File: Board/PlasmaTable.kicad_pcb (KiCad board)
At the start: 2 copper layers, 99.1 x 86.4 mm, 48 parts, among them P1 CONN_20X2, P10 CONN_1, P11 CONN_1, P2 CONN_5, P3 CONN_5, P4 CONN_5, P5 CONN_5, P6 CONN_5, P7 CONN_5, P8 CONN_1, P9 CONN_1, Q1 TIP120, Q2 TIP120, Q3 TIP120, U1 7805, U2 7805, U3 7805, U4 7805

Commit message: Plotted PCB
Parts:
- C1, C4: value C -> 47 uF
- C2, C5: value C -> 100 uF
- C3, C6: value C -> 1000 uF
- C7, C8, C9: value C -> 0.1 uF
- R1, R12, R8: value R -> 51K
- R10, R14, R3, R5, R6, R7: value R -> 10K
- R11, R13, R15, R2, R4, R9: value R -> 0.2 Ohm
- moved DRV1 36.5 mm to (157.5, 99.1)
- moved DRV3 29.6 mm to (127.0, 99.1)
- moved D2 6.50 mm to (148.0, 115.9), turned to 180 degrees
- moved D1 6.46 mm to (161.9, 116.0), turned to 180 degrees
- moved D3 5.88 mm to (134.9, 116.0), turned to 180 degrees
- moved DRV2 3.44 mm to (142.2, 99.1)
- moved R1 3.24 mm to (172.7, 98.2)
- moved R10 3.24 mm to (172.7, 108.3)
- moved R11 3.24 mm to (172.7, 90.5)
- moved R12 3.24 mm to (172.7, 121.0)
- moved R13 3.24 mm to (172.7, 95.6)
- moved R15 3.24 mm to (172.7, 85.5)
- moved R2 3.24 mm to (172.7, 100.7)
- moved R3 3.24 mm to (172.7, 103.2)
- moved R6 3.24 mm to (172.7, 118.5)
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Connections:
- P2 pad 2: /OUT1B_X -> /OUT2A_X
- P2 pad 3: /OUT2A_X -> /OUT1B_X
- P3 pad 2: /OUT1B_Y -> /OUT2A_Y
- P3 pad 3: /OUT2A_Y -> /OUT1B_Y
- P4 pad 2: /OUT1B_Z -> /OUT2A_Z
- P4 pad 3: /OUT2A_Z -> /OUT1B_Z
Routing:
- net GND: track 0.00 -> 1024.8 mm, vias 0 -> 6
- net Net-(DRV1-Pad23): track 0.00 -> 435.7 mm, vias 0 -> 2
- net /AUX1_BASE: track 0.00 -> 212.0 mm
- net VCC: track 0.00 -> 199.4 mm, vias 0 -> 8
- net /AUX2: track 0.00 -> 194.8 mm
- net +5V: track 0.00 -> 175.4 mm, vias 0 -> 5
- net /AUX1: track 0.00 -> 164.8 mm
- net /SWITCH2: track 0.00 -> 149.8 mm, vias 0 -> 2
- net Net-(DRV3-Pad15): track 0.00 -> 139.0 mm, vias 0 -> 2
- net Net-(DRV3-Pad11): track 0.00 -> 138.4 mm, vias 0 -> 2
- net /SWITCH3: track 0.00 -> 135.7 mm, vias 0 -> 2
- net /SWITCH1: track 0.00 -> 133.2 mm
- net /Z_ENABLE: track 0.00 -> 130.5 mm
- net Net-(Q2-Pad1): track 0.00 -> 116.4 mm
- net Net-(DRV2-Pad11): track 0.00 -> 112.3 mm, vias 0 -> 3
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- added copper zone on B.Cu, net GND
- added copper zone on F.Cu, net GND
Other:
- rule trace_min: 0.2 -> 0.1016
- board text added: "1"
- board text added: "5V"
- board text added: "A+"
- board text added: "A-"
- board text added: "AUX"
- board text added: "B+"
- board text added: "B-"
- board text added: "DISCRETE"
- board text added: "G"
- board text added: "S1"
- board text added: "S2"
- board text added: "S3"
- board text added: "SWITCHES"
- board text added: "V+"
- board text added: "VIN"
- board text added: "X AXIS"
- board text added: "X1"
- board text added: "X2"
- board text added: "X3"
- board text added: "Y AXIS"
- board text added: "Z AXIS"

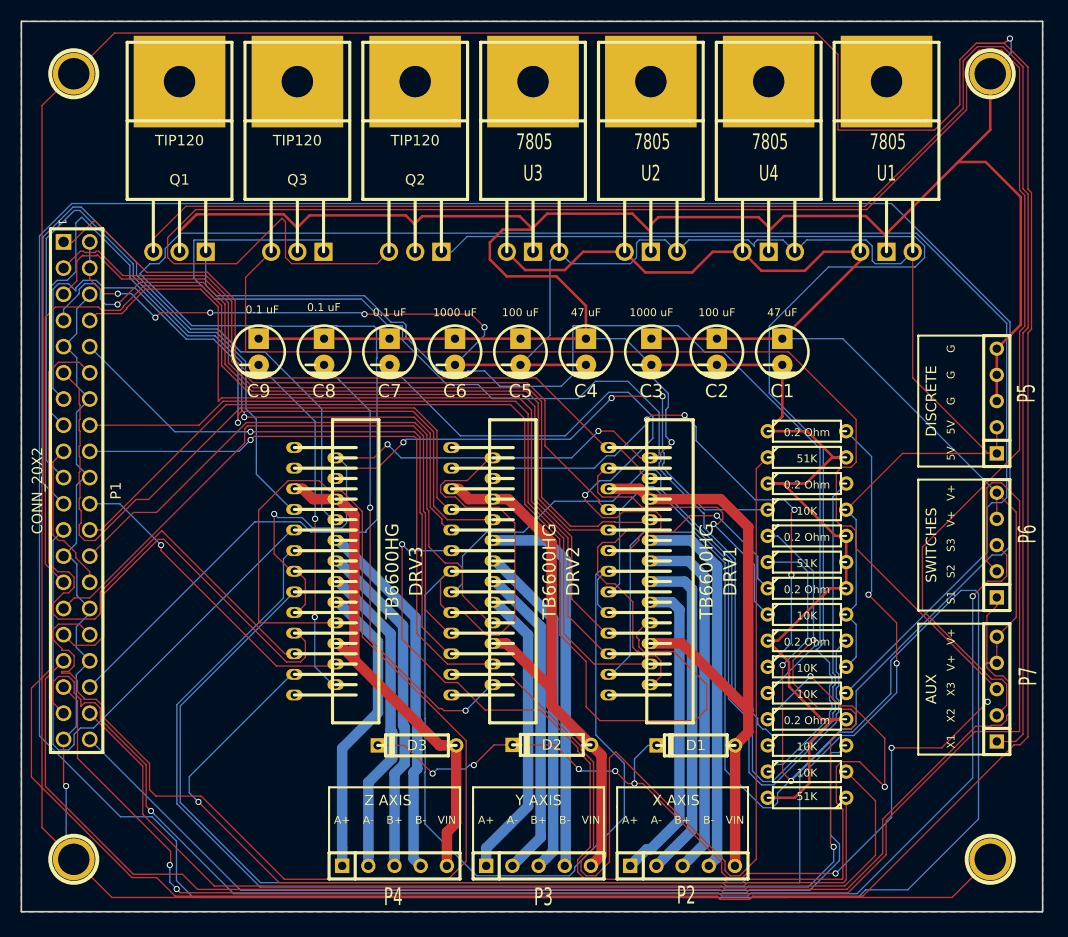
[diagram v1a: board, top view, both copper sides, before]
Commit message: Fixed errors made in first revision and plotted
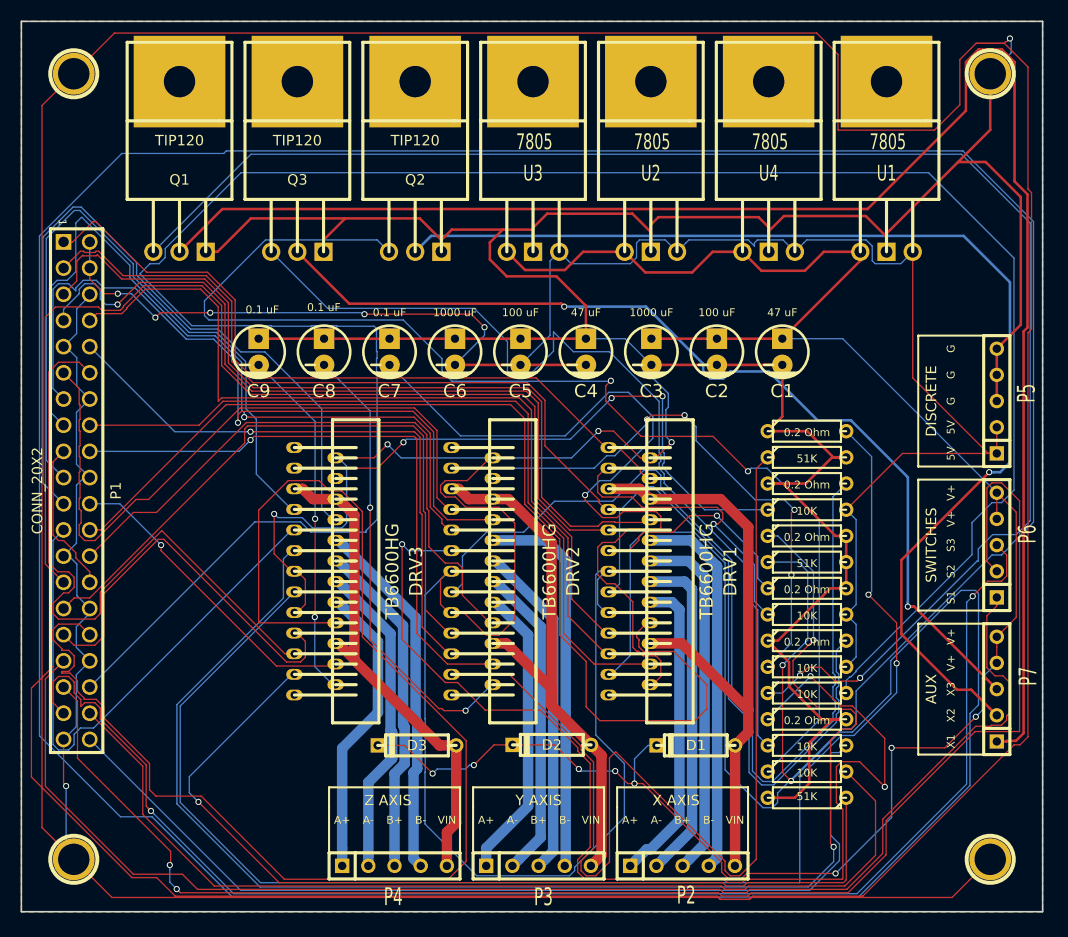
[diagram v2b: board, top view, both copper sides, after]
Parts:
- Q1, Q2, Q3: footprint discret:TO220 -> PlasmaTable:TO220
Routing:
- net /AUX2: track 194.8 -> 111.8 mm, vias 0 -> 1
- net Net-(Q1-Pad1): track 104.2 -> 154.8 mm, vias 0 -> 2
- net Net-(Q3-Pad1): track 107.6 -> 88.0 mm
- net /AUX3: track 107.1 -> 93.8 mm, vias 0 -> 3
- net GND: track 1024.8 -> 1012.3 mm
- net /AUX1_BASE: track 212.0 -> 221.6 mm
- net Net-(DRV1-Pad23): track 435.7 -> 444.2 mm
- net /AUX1: track 164.8 -> 161.1 mm
- net Net-(Q2-Pad1): track 116.4 -> 119.4 mm, vias 0 -> 2
- net VCC: track 199.4 -> 198.7 mm

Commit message: Got board layed out
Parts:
- added C10: C, smd_capacitors:c_0603, F.Cu at (182.5, 68.8)
- added C11: C, smd_capacitors:c_0603, F.Cu at (182.5, 70.3)
- added C12: C, smd_capacitors:c_0603, F.Cu at (182.5, 71.8)
- added C13: 0.1 uF, smd_capacitors:c_0603, F.Cu at (182.5, 73.3)
- added C14: 47 uF, smd_capacitors:c_0603, F.Cu at (182.5, 74.8)
- added C15: 100 uF, smd_capacitors:c_0603, F.Cu at (182.5, 76.3)
- added C16: 1000 uF, smd_capacitors:c_0603, F.Cu at (182.5, 77.8)
- added C17: C, smd_capacitors:c_0603, F.Cu at (182.5, 79.3)
- added C18: C, smd_capacitors:c_0603, F.Cu at (182.5, 80.8)
- added C19: C, smd_capacitors:c_0603, F.Cu at (182.5, 82.3)
- added C20: C, smd_capacitors:c_0603, F.Cu at (182.5, 83.8)
- added C21: 47 uF, smd_capacitors:c_0603, F.Cu at (182.5, 85.3)
- added C22: 100 uF, smd_capacitors:c_0603, F.Cu at (182.5, 86.8)
- added C23: 1000 uF, smd_capacitors:c_0603, F.Cu at (182.5, 88.3)
- added C24: C, smd_capacitors:c_0603, F.Cu at (182.5, 89.8)
- added C25: C, smd_capacitors:c_0603, F.Cu at (182.5, 91.3)
- added C26: C, smd_capacitors:c_0603, F.Cu at (182.5, 92.8)
- added C27: C, smd_capacitors:c_0603, F.Cu at (182.5, 94.3)
- added C28: C, smd_capacitors:c_0603, F.Cu at (182.5, 95.8)
- added C29: C, smd_capacitors:c_0603, F.Cu at (182.5, 97.3)
- added C30: C, smd_capacitors:c_0603, F.Cu at (182.5, 98.8)
- added C31: C, smd_capacitors:c_0603, F.Cu at (182.5, 100.3)
- added C32: 0.1 uF, smd_capacitors:c_0603, F.Cu at (182.5, 101.8)
- added C33: 0.1 uF, smd_capacitors:c_0603, F.Cu at (182.5, 103.3)
- added C34: C, smd_capacitors:c_0603, F.Cu at (182.5, 104.8)
- added C35: C, smd_capacitors:c_0603, F.Cu at (182.5, 106.3)
- added C36: C, smd_capacitors:c_0603, F.Cu at (182.5, 107.8)
- added C37: C, smd_capacitors:c_0603, F.Cu at (182.5, 109.3)
- added C38: C, smd_capacitors:c_0603, F.Cu at (182.5, 110.8)
- added CON1: BARREL_JACK, connect:BARREL_JACK, F.Cu at (82.3, 35.0)
- added D10: DIODESCH, w_smd_leds:Led_1206, F.Cu at (110.7, 107.3)
- added D11: DIODESCH, w_smd_leds:Led_1206, F.Cu at (110.6, 110.6)
- added D12: Z STEP, w_smd_leds:Led_1206, F.Cu at (144.8, 73.6)
- added D13: Z DIR, w_smd_leds:Led_1206, F.Cu at (165.1, 73.7)
- added D14: DIODESCH, w_smd_leds:Led_1206, F.Cu at (110.7, 114.0)
- added D15: DIODESCH, w_smd_leds:Led_1206, F.Cu at (140.8, 104.1)
- added D16: DIODESCH, w_smd_leds:Led_1206, F.Cu at (140.8, 107.4)
- added D17: DIODESCH, w_smd_leds:Led_1206, F.Cu at (140.8, 110.7)
- added D18: DIODESCH, w_smd_leds:Led_1206, F.Cu at (140.7, 114.0)
- added D19: 30V TVS, w_smd_leds:Led_1206, F.Cu at (80.5, 52.6)
- added D4: Y DIR, w_smd_leds:Led_1206, F.Cu at (134.6, 73.7)
- added D5: DIODESCH, w_smd_leds:Led_1206, F.Cu at (78.2, 104.0)
- added D6: DIODESCH, w_smd_leds:Led_1206, F.Cu at (78.2, 107.3)
- added D7: DIODESCH, w_smd_leds:Led_1206, F.Cu at (78.3, 110.6)
- added D8: DIODESCH, w_smd_leds:Led_1206, F.Cu at (78.3, 114.0)
- added D9: DIODESCH, w_smd_leds:Led_1206, F.Cu at (110.8, 104.0)
- added J1: USB, connect:USB_B, F.Cu at (67.3, 37.5)
- added Q4: DARL_N, PlasmaTable:TO-252-3, F.Cu at (122.3, 40.7)
- added Q5: DARL_N, PlasmaTable:TO-252-3, F.Cu at (132.3, 40.7)
- added R16: 10K, smd_resistors:r_2010, F.Cu at (141.8, 56.1)
- added R17: 10K, smd_resistors:r_2010, F.Cu at (145.3, 56.1)
- added RV1: POT, PlasmaTable:TRIM_POT, F.Cu at (96.5, 73.7)
- added RV2: POT, PlasmaTable:TRIM_POT, F.Cu at (124.5, 73.7)
- added RV3: POT, PlasmaTable:TRIM_POT, F.Cu at (154.9, 73.7)
- added U5: 7805, PlasmaTable:7805_DPAK, F.Cu at (172.3, 40.7)
- C1, C4: value 47 uF -> C; footprint capacitors:CP_5x11mm -> smd_capacitors:c_0603
- C2, C5: value 100 uF -> C; footprint capacitors:CP_5x11mm -> smd_capacitors:c_0603
- C3: value 1000 uF -> C; footprint capacitors:CP_5x11mm -> smd_capacitors:c_0603
- C6: value 1000 uF -> 0.1uF; footprint capacitors:CP_5x11mm -> smd_capacitors:c_0603
- C7: value 0.1 uF -> 0.1uF; footprint capacitors:CP_5x11mm -> smd_capacitors:c_0603
- C8, C9: value 0.1 uF -> C; footprint capacitors:CP_5x11mm -> smd_capacitors:c_0603
- D1: value DIODE -> X STEP; footprint discret:D3 -> w_smd_leds:Led_1206
- D2: value DIODE -> X DIR; footprint discret:D3 -> w_smd_leds:Led_1206
- D3: value DIODE -> Y STEP; footprint discret:D3 -> w_smd_leds:Led_1206
- P1: value CONN_20X2 -> CONN_5; footprint pin_array:PIN_ARRAY_20X2 -> connect:SIL-5
- P10, P11, P8, P9: footprint connect:1pin -> PlasmaTable:BOLT_HOLE
- Q1, Q2, Q3: value TIP120 -> DARL_N; footprint PlasmaTable:TO220 -> PlasmaTable:TO-252-3
- R1, R14, R2, R3, R4, R7: footprint discret:R3 -> smd_resistors:r_2010
- R10, R6: value 10K -> 0.2 Ohm; footprint discret:R3 -> smd_resistors:r_2010
- R11, R13, R15: value 0.2 Ohm -> 10K; footprint discret:R3 -> smd_resistors:r_2010
- R12, R8: value 51K -> 0.2 Ohm; footprint discret:R3 -> smd_resistors:r_2010
- R5: value 10K -> 51K; footprint discret:R3 -> smd_resistors:r_2010
- R9: value 0.2 Ohm -> 51K; footprint discret:R3 -> smd_resistors:r_2010
- U1: value 7805 -> PHOTON; footprint discret:LM78XX -> PlasmaTable:PHOTON_SMD
- U2, U3, U4: footprint discret:LM78XX -> PlasmaTable:7805_DPAK
- moved P10 140.3 mm to (50.8, 38.1)
- moved U1 128.7 mm to (54.4, 93.7), turned to 0 degrees
- moved P11 117.1 mm to (190.5, 127.0)
- moved R1 93.4 mm to (89.3, 56.1), turned to 90 degrees
- moved R2 91.5 mm to (92.8, 56.1), turned to 90 degrees
- moved R6 90.8 mm to (106.8, 56.1), turned to 90 degrees
- moved R3 89.8 mm to (96.3, 56.1), turned to 90 degrees
- moved P8 89.5 mm to (190.5, 37.5)
- moved R5 88.4 mm to (103.3, 56.1), turned to 90 degrees
- moved R4 88.3 mm to (99.8, 56.1), turned to 90 degrees
- moved D1 86.6 mm to (86.4, 73.7), turned to 90 degrees
- moved R7 86.5 mm to (110.3, 56.1), turned to 90 degrees
- moved R9 79.7 mm to (117.3, 56.1), turned to 90 degrees
- moved R12 79.0 mm to (127.8, 56.1), turned to 90 degrees
- moved R10 73.7 mm to (120.8, 56.1), turned to 90 degrees
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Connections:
- C1 pad 1: VCC -> GND
- C1 pad 2: GND -> /AUX5
- C2 pad 1: VCC -> GND
- C2 pad 2: GND -> /AUX4
- C3 pad 1: VCC -> GND
- C3 pad 2: GND -> /AUX3
- C4 pad 2: +5V -> /AUX2
- C5 pad 2: +5V -> /AUX1
- C6 pad 2: +5V -> Net-(C6-Pad2)
- C8 pad 2: Net-(C8-Pad2) -> /SWITCH5
- C9 pad 2: Net-(C9-Pad2) -> /SWITCH4
- D1 pad 1: /X_VIN -> /X_STEP
- D1 pad 2: VCC -> Net-(D1-Pad2)
- D2 pad 1: /Y_VIN -> /X_DIR
- D2 pad 2: VCC -> Net-(D2-Pad2)
- D3 pad 1: /Z_VIN -> /Y_STEP
- D3 pad 2: VCC -> Net-(D3-Pad2)
- DRV1 pad 18: /X_ENABLE -> /DRV_ENABLE
- DRV1 pad 19: /X_RESET -> (no net)
- DRV1 pad 20: /X_VIN -> +24V
- DRV1 pad 21: /X_STEP -> Net-(D1-Pad2)
- DRV1 pad 22: /X_DIR -> Net-(D2-Pad2)
- DRV1 pad 24: Net-(C7-Pad2) -> Net-(C13-Pad2)
- DRV1 pad 4: (no net) -> GND
- DRV1 pad 5: /X_VIN -> Net-(DRV1-Pad5)
- DRV1 pad 6: /X_VIN -> +24V
- DRV1 pad 7: /X_M1 -> Net-(DRV1-Pad3)
- DRV1 pad 8: /X_M2 -> GND
- DRV1 pad 9: /X_M3 -> Net-(DRV1-Pad3)
- DRV2 pad 18: /Y_ENABLE -> /DRV_ENABLE
- DRV2 pad 19: /Y_RESET -> (no net)
- DRV2 pad 20: /Y_VIN -> +24V
- DRV2 pad 21: /Y_STEP -> Net-(D3-Pad2)
- DRV2 pad 22: /Y_DIR -> Net-(D4-Pad2)
- DRV2 pad 24: Net-(C8-Pad2) -> Net-(C32-Pad2)
- DRV2 pad 4: (no net) -> GND
- DRV2 pad 5: /Y_VIN -> Net-(DRV2-Pad5)
- DRV2 pad 6: /Y_VIN -> +24V
- DRV2 pad 7: /Y_M1 -> Net-(DRV2-Pad3)
- DRV2 pad 8: /Y_M2 -> GND
- DRV2 pad 9: /Y_M3 -> Net-(DRV2-Pad3)
- DRV3 pad 18: /Z_ENABLE -> /DRV_ENABLE
- DRV3 pad 19: /Z_RESET -> (no net)
- DRV3 pad 20: /Z_VIN -> +24V
- DRV3 pad 21: /Z_STEP -> Net-(D12-Pad2)
- DRV3 pad 22: /Z_DIR -> Net-(D13-Pad2)
- DRV3 pad 24: Net-(C9-Pad2) -> Net-(C33-Pad2)
- DRV3 pad 4: (no net) -> GND
- DRV3 pad 5: /Z_VIN -> Net-(DRV3-Pad5)
- DRV3 pad 6: /Z_VIN -> +24V
- DRV3 pad 7: /Z_M1 -> Net-(DRV3-Pad3)
- DRV3 pad 8: /Z_M2 -> GND
- DRV3 pad 9: /Z_M3 -> Net-(DRV3-Pad3)
- P1 pad 1: (no net) -> /AUX1
- P1 pad 2: +5V -> /AUX2
- P1 pad 3: /X_M1 -> /AUX3
- P1 pad 4: +5V -> /AUX4
- P1 pad 5: /X_M2 -> /AUX5
- P2 pad 1: /OUT1A_X -> /SWITCH6
- P2 pad 2: /OUT2A_X -> +24V
- P2 pad 3: /OUT1B_X -> +24V
- P2 pad 4: /OUT2B_X -> +24V
- P2 pad 5: /X_VIN -> +24V
- P3 pad 1: /OUT1A_Y -> /SWITCH1
- P3 pad 2: /OUT2A_Y -> /SWITCH2
- P3 pad 3: /OUT1B_Y -> /SWITCH3
- P3 pad 4: /OUT2B_Y -> /SWITCH4
- P3 pad 5: /Y_VIN -> /SWITCH5
- P4 pad 1: /OUT1A_Z -> +5V
- P4 pad 2: /OUT2A_Z -> +5V
- P4 pad 3: /OUT1B_Z -> +5V
- P4 pad 4: /OUT2B_Z -> +3.3V
- P4 pad 5: /Z_VIN -> +3.3V
- P5 pad 1: +5V -> /OUT1A_Z
- P5 pad 2: +5V -> /OUT2A_Z
- P5 pad 3: GND -> /OUT1B_Z
- P5 pad 4: GND -> /OUT2B_Z
- P6 pad 1: /SWITCH1 -> /OUT1A_Y
- P6 pad 2: /SWITCH2 -> /OUT2A_Y
- P6 pad 3: /SWITCH3 -> /OUT1B_Y
- P6 pad 4: VCC -> /OUT2B_Y
- P6 pad 5: VCC -> GND
- P7 pad 1: /AUX1 -> /OUT1A_X
- P7 pad 2: /AUX2 -> /OUT2A_X
- P7 pad 3: /AUX3 -> /OUT1B_X
- P7 pad 4: VCC -> /OUT2B_X
- P7 pad 5: VCC -> GND
- Q1 pad 1: Net-(Q1-Pad1) -> GND
- Q1 pad 2: /AUX1 -> Net-(C34-Pad2)
- Q1 pad 3: GND -> /AUX5
- Q2 pad 1: Net-(Q2-Pad1) -> GND
- Q2 pad 2: /AUX2 -> Net-(C35-Pad2)
- Q2 pad 3: GND -> /AUX4
- Q3 pad 1: Net-(Q3-Pad1) -> GND
- Q3 pad 2: /AUX3 -> Net-(C36-Pad2)
- Q3 pad 3: GND -> /AUX3
- R10 pad 1: Net-(DRV2-Pad3) -> Net-(DRV3-Pad11)
- R10 pad 2: +5V -> GND
- R11 pad 1: GND -> Net-(DRV3-Pad3)
- R11 pad 2: Net-(DRV2-Pad15) -> +5V
- R12 pad 1: Net-(DRV3-Pad23) -> GND
- R12 pad 2: GND -> Net-(DRV3-Pad15)
- R13 pad 1: Net-(DRV3-Pad11) -> Net-(C34-Pad2)
- R13 pad 2: GND -> /AUX5_BASE
- R14 pad 1: Net-(DRV3-Pad3) -> Net-(C35-Pad2)
- R14 pad 2: +5V -> /AUX4_BASE
- R15 pad 1: GND -> Net-(C36-Pad2)
- R15 pad 2: Net-(DRV3-Pad15) -> /AUX3_BASE
- R5 pad 1: Net-(Q1-Pad1) -> Net-(DRV2-Pad23)
- R5 pad 2: /AUX1_BASE -> GND
- R6 pad 1: Net-(Q2-Pad1) -> Net-(DRV2-Pad11)
- R6 pad 2: /AUX2_BASE -> GND
- R7 pad 1: Net-(Q3-Pad1) -> Net-(DRV2-Pad3)
- R7 pad 2: /AUX3_BASE -> +5V
- R8 pad 1: Net-(DRV2-Pad23) -> GND
- R8 pad 2: GND -> Net-(DRV2-Pad15)
- R9 pad 1: Net-(DRV2-Pad11) -> Net-(DRV3-Pad23)
- U1 pad 4: (no net) -> /AUX4_BASE
- U2 pad VI: VCC -> +24V
- U3 pad VI: VCC -> +24V
- U4 pad VI: VCC -> +24V
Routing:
- net GND: track 1012.3 -> 0.00 mm, vias 6 -> 0
- net Net-(DRV1-Pad23): track 444.2 -> 0.00 mm, vias 2 -> 0
- net /AUX1_BASE: track 221.6 -> 0.00 mm
- net VCC: track 198.7 -> 0.00 mm, vias 8 -> 0
- net +5V: track 175.4 -> 0.00 mm, vias 5 -> 0
- net /AUX1: track 161.1 -> 0.00 mm
- net Net-(Q1-Pad1): track 154.8 -> 0.00 mm, vias 2 -> 0
- net /SWITCH2: track 149.8 -> 0.00 mm, vias 2 -> 0
- net Net-(DRV3-Pad15): track 139.0 -> 0.00 mm, vias 2 -> 0
- net Net-(DRV3-Pad11): track 138.4 -> 0.00 mm, vias 2 -> 0
- net /SWITCH3: track 135.7 -> 0.00 mm, vias 2 -> 0
- net /SWITCH1: track 133.2 -> 0.00 mm
- net /Z_ENABLE: track 130.5 -> 0.00 mm
- net Net-(Q2-Pad1): track 119.4 -> 0.00 mm, vias 2 -> 0
- net Net-(DRV2-Pad11): track 112.3 -> 0.00 mm, vias 3 -> 0
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- removed copper zone on B.Cu, net GND
- removed copper zone on F.Cu, net GND
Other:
- board outline removed
- board text added: "X"
- board text added: "Y"
- board text added: "Z"
- board text removed: "1"
- board text removed: "5V"
- board text removed: "A+"
- board text removed: "A-"
- board text removed: "AUX"
- board text removed: "B+"
- board text removed: "B-"
- board text removed: "DISCRETE"
- board text removed: "G"
- board text removed: "S1"
- board text removed: "S2"
- board text removed: "S3"
- board text removed: "SWITCHES"
- board text removed: "V+"
- board text removed: "VIN"
- board text removed: "X AXIS"
- board text removed: "X1"
- board text removed: "X2"
- board text removed: "X3"
- board text removed: "Y AXIS"
- board text removed: "Z AXIS"

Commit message: Locked down board layout
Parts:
- P1, P2, P3, P4, P5, P6, P7: footprint connect:SIL-5 -> PlasmaTable:PLUGABLE_HEADER
- moved P5 60.8 mm to (198.1, 138.4)
- moved P4 49.3 mm to (74.9, 116.8), turned to 270 degrees
- moved P1 42.2 mm to (118.1, 138.4)
- moved R1 41.1 mm to (129.3, 65.6)
- moved R10 41.1 mm to (160.8, 65.6)
- moved R11 41.1 mm to (164.3, 65.6)
- moved R12 41.1 mm to (167.8, 65.6)
- moved R2 41.1 mm to (132.8, 65.6)
- moved R3 41.1 mm to (136.3, 65.6)
- moved R4 41.1 mm to (139.8, 65.6)
- moved R5 41.1 mm to (143.3, 65.6)
- moved R6 41.1 mm to (146.8, 65.6)
- moved R7 41.1 mm to (150.3, 65.6)
- moved R8 41.1 mm to (153.8, 65.6)
- moved R9 41.1 mm to (157.3, 65.6)
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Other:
- board outline added: 152.4 x 104.1 mm

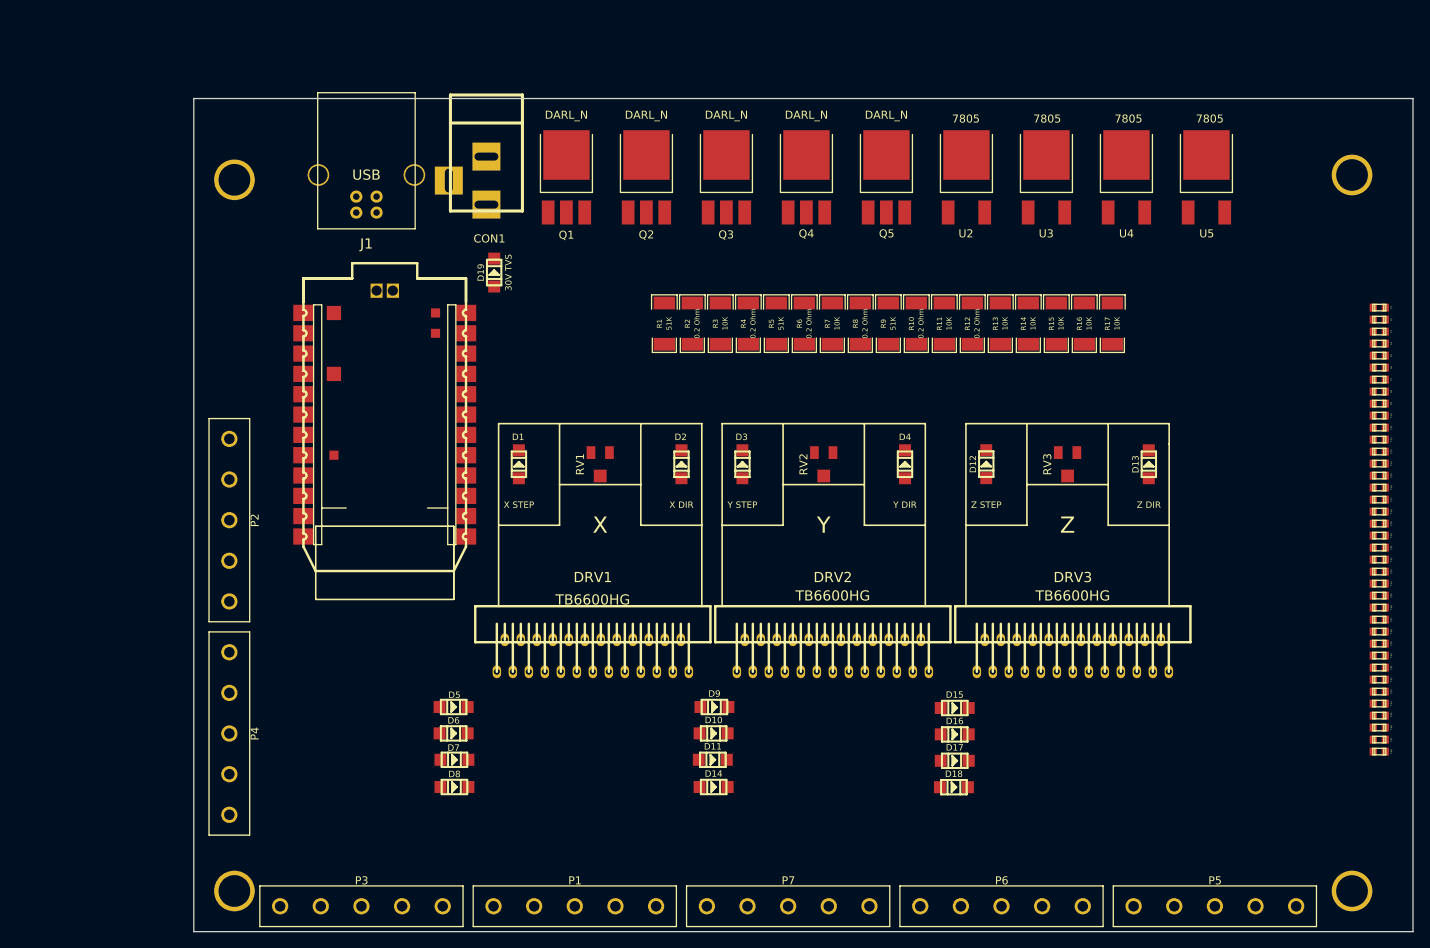
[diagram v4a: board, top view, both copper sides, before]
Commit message: Just about finished routing
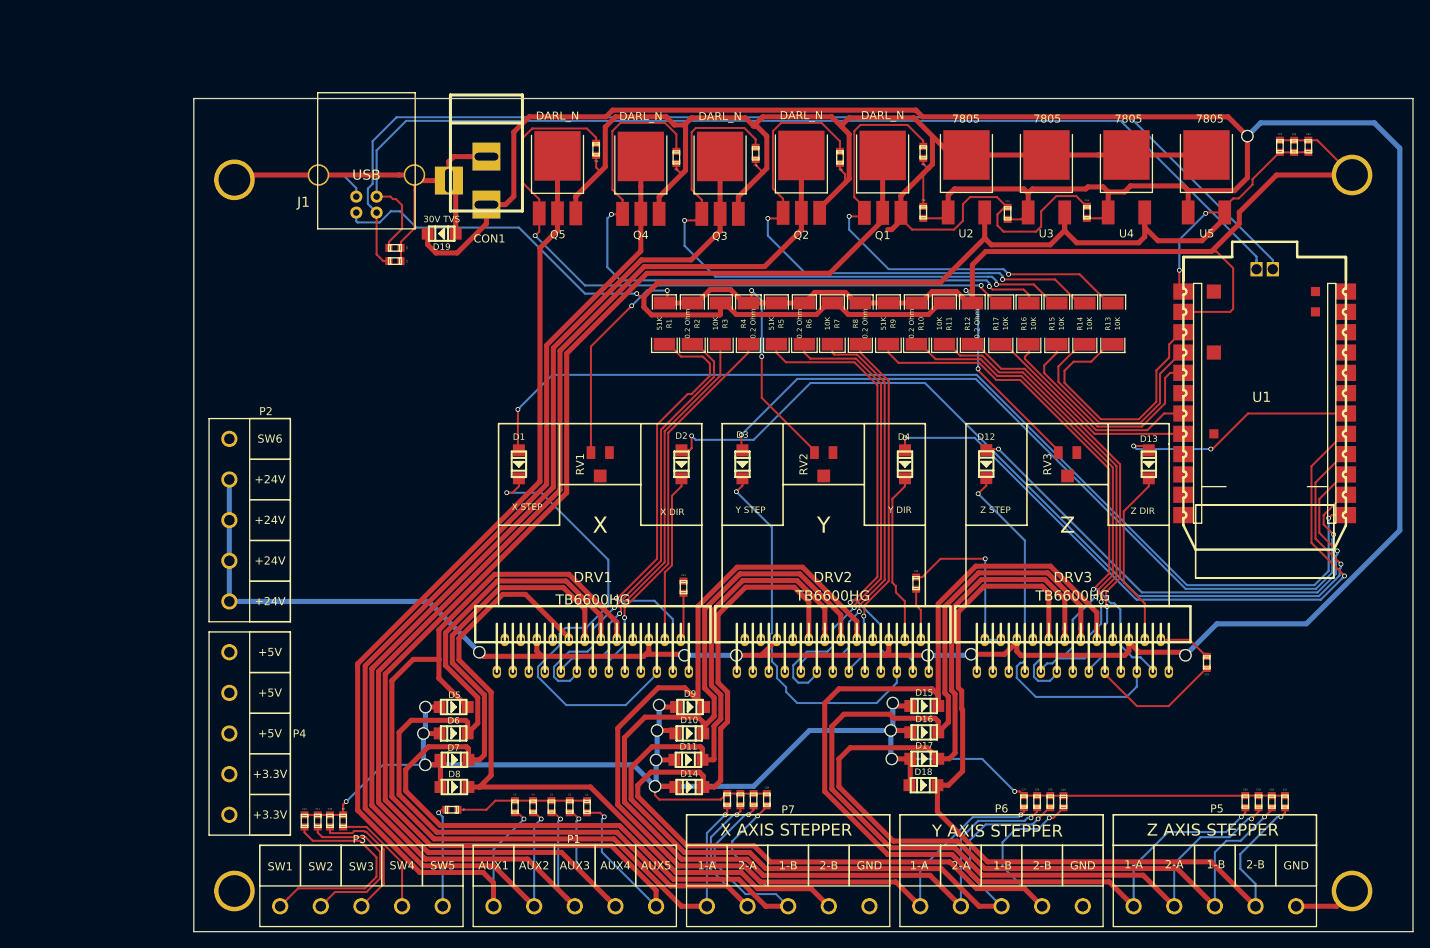
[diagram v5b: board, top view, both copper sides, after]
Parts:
- moved C12 142.6 mm to (84.3, 127.8), turned to 90 degrees
- moved C11 141.5 mm to (86.0, 127.8), turned to 90 degrees
- moved C10 140.6 mm to (87.5, 127.8), turned to 90 degrees
- moved C9 139.6 mm to (89.2, 127.8), turned to 90 degrees
- moved C8 127.2 mm to (102.7, 126.4)
- moved C6 123.9 mm to (95.6, 56.1)
- moved C7 123.9 mm to (95.6, 57.8)
- moved C38 123.5 mm to (120.8, 43.8), turned to 270 degrees
- moved C5 121.9 mm to (110.6, 126.0), turned to 90 degrees
- moved C4 120.6 mm to (112.9, 126.0), turned to 90 degrees
- moved C3 119.3 mm to (115.2, 126.0), turned to 90 degrees
- moved C2 118.1 mm to (117.5, 126.0), turned to 90 degrees
- moved C1 117.1 mm to (119.6, 126.0), turned to 90 degrees
- moved C37 114.1 mm to (130.8, 44.8), turned to 270 degrees
- moved U1 110.0 mm to (194.2, 93.9)
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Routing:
- net GND: track 0.00 -> 724.2 mm, vias 0 -> 19
- net +24V: track 0.00 -> 437.4 mm, vias 0 -> 7
- net +5V: track 0.00 -> 206.3 mm, vias 0 -> 3
- net /AUX5: track 0.00 -> 176.7 mm, vias 0 -> 1
- net /AUX4: track 0.00 -> 161.1 mm, vias 0 -> 1
- net /AUX3: track 0.00 -> 146.7 mm, vias 0 -> 1
- net Net-(C7-Pad2): track 0.00 -> 139.0 mm
- net Net-(C6-Pad2): track 0.00 -> 136.7 mm
- net /OUT1A_Z: track 0.00 -> 134.9 mm, vias 0 -> 1
- net /AUX2: track 0.00 -> 134.6 mm, vias 0 -> 1
- net /OUT2A_Z: track 0.00 -> 132.6 mm, vias 0 -> 1
- net /OUT1B_Y: track 0.00 -> 130.8 mm, vias 0 -> 1
- net /OUT1B_X: track 0.00 -> 130.7 mm, vias 0 -> 1
- net /OUT2B_Y: track 0.00 -> 130.1 mm, vias 0 -> 1
- net /AUX1: track 0.00 -> 129.8 mm, vias 0 -> 1
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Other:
- board text added: "+24V"
- board text added: "+3.3V"
- board text added: "+5V"
- board text added: "1-A"
- board text added: "1-B"
- board text added: "2-A"
- board text added: "2-B"
- board text added: "AUX1"
- board text added: "AUX2"
- board text added: "AUX3"
- board text added: "AUX4"
- board text added: "AUX5"
- board text added: "GND"
- board text added: "SW1"
- board text added: "SW2"
- board text added: "SW3"
- board text added: "SW4"
- board text added: "SW5"
- board text added: "SW6"
- board text added: "X AXIS STEPPER"
- board text added: "Y AXIS STEPPER"
- board text added: "Z AXIS STEPPER"
